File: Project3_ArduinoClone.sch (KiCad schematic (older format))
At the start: 13 parts, among them U1 24LC1025, U2 24LC1025, U3 DS1337_v1, U4 ATMEGA328P-AU, Y1 Crystal, Y2 Crystal

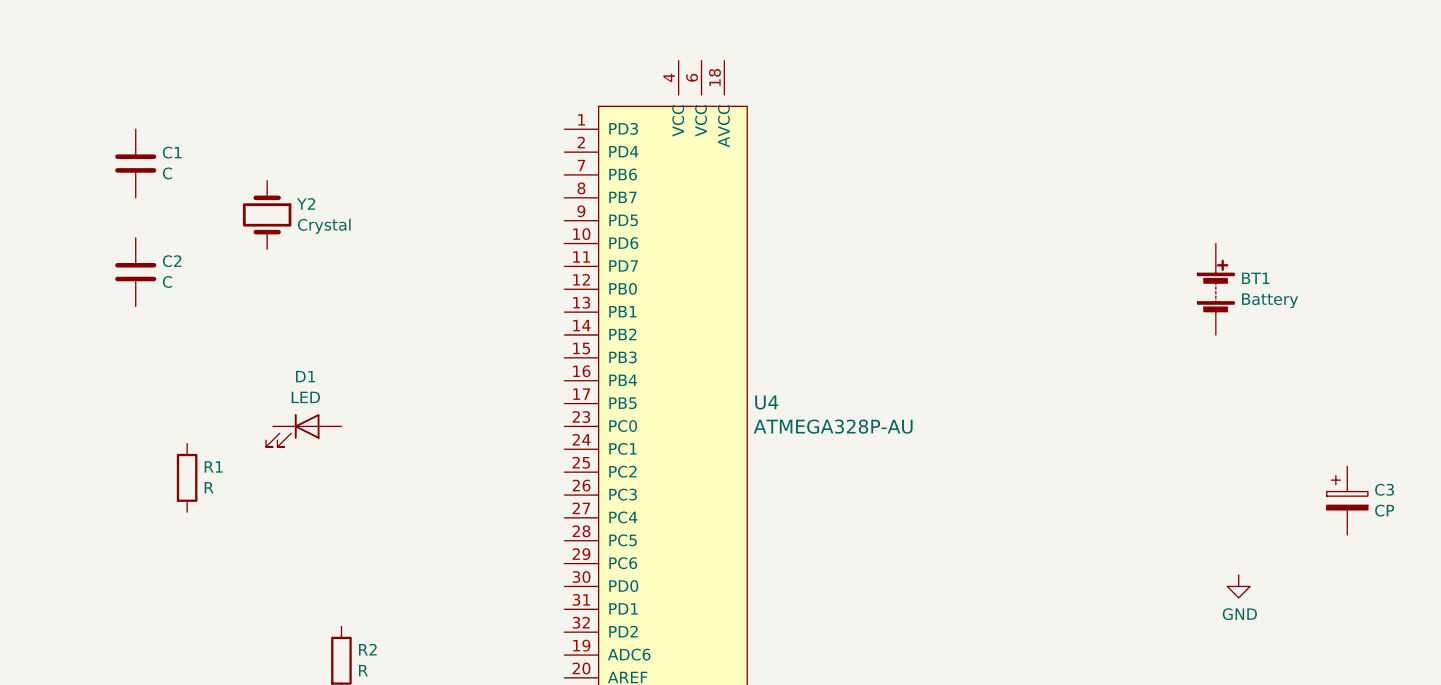
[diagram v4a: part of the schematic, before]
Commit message: Footprints assigned.
Review with real footprints that I'm going to use.
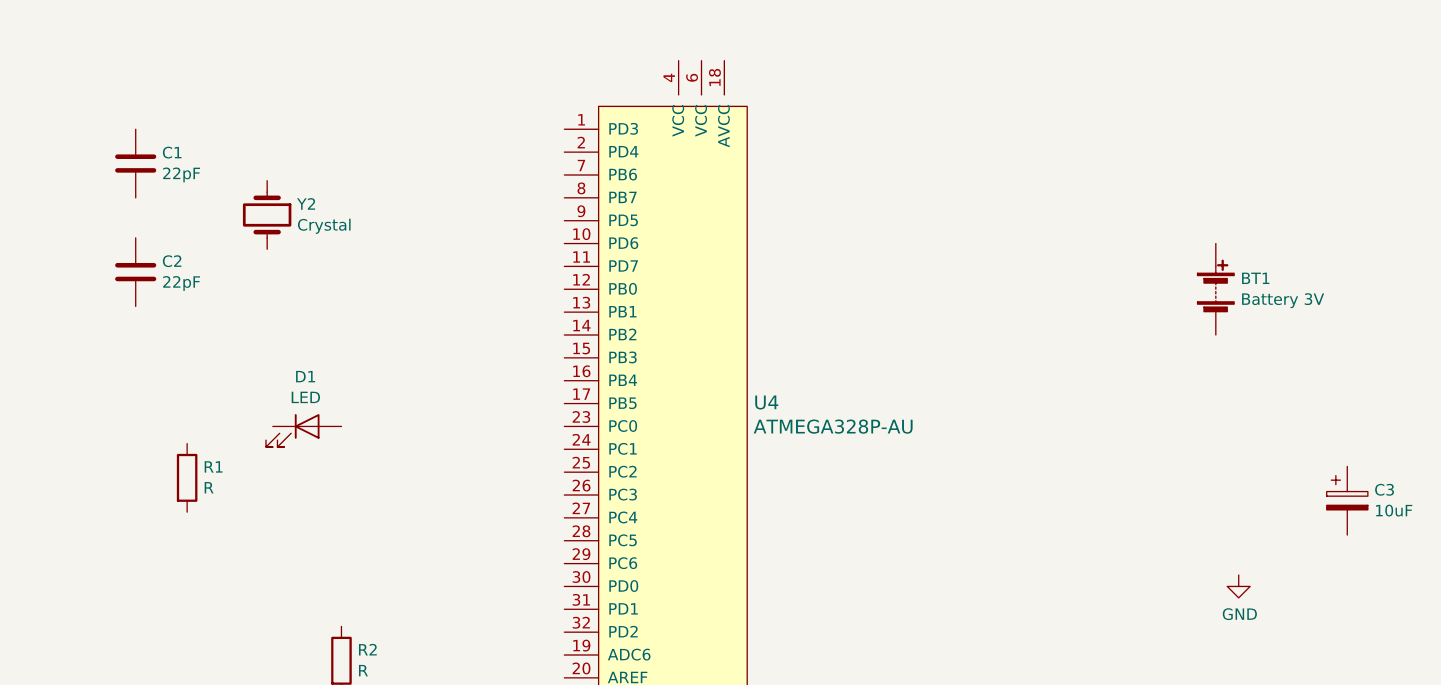
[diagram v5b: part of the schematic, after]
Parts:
- BT1: value Battery -> Battery 3V; footprint (none) -> Connector_PinHeader_2.54mm:PinHeader_1x02_P2.54mm_Vertical
- C1, C2: value C -> 22pF; footprint (none) -> Capacitor_SMD:C_0805_2012Metric_Pad1.15x1.40mm_HandSolder
- C3: value CP -> 10uF; footprint (none) -> Capacitor_SMD:C_0805_2012Metric_Pad1.15x1.40mm_HandSolder
- D1: footprint (none) -> LED_SMD:LED_0805_2012Metric_Pad1.15x1.40mm_HandSolder
- R1, R2: footprint (none) -> Resistor_SMD:R_0805_2012Metric_Pad1.15x1.40mm_HandSolder
- U1, U2: footprint (none) -> Package_SO:SOIJ-8_5.3x5.3mm_P1.27mm
- U3: footprint (none) -> Package_SO:SO-8_5.3x6.2mm_P1.27mm
- Y1: footprint (none) -> Crystal:Crystal_SMD_MicroCrystal_CC7V-T1A-2Pin_3.2x1.5mm_HandSoldering
- Y2: footprint (none) -> Crystal:Crystal_SMD_5032-2Pin_5.0x3.2mm_HandSoldering
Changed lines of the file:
@@
 P 9450 2975
 F 0 "BT1" H 9558 3021 50  0000 L CNN
-F 1 "Battery" H 9558 2930 50  0000 L CNN
-F 2 "" V 9450 3035 50  0001 C CNN
+F 1 "Battery 3V" H 9558 2930 50  0000 L CNN
+F 2 "Connector_PinHeader_2.54mm:PinHeader_1x02_P2.54mm_Vertical" V 9450 3035 50  0001 C CNN
 F 3 "~" V 9450 3035 50  0001 C CNN
 	1    9450 2975
@@
 P 4725 2425
 F 0 "C1" H 4840 2471 50  0000 L CNN
-F 1 "C" H 4840 2380 50  0000 L CNN
-F 2 "" H 4763 2275 50  0001 C CNN
+F 1 "22pF" H 4840 2380 50  0000 L CNN
+F 2 "Capacitor_SMD:C_0805_2012Metric_Pad1.15x1.40mm_HandSolder" H 4763 2275 50  0001 C CNN
 F 3 "~" H 4725 2425 50  0001 C CNN
 	1    4725 2425
@@
 P 4725 2900
 F 0 "C2" H 4840 2946 50  0000 L CNN
-F 1 "C" H 4840 2855 50  0000 L CNN
-F 2 "" H 4763 2750 50  0001 C CNN
+F 1 "22pF" H 4840 2855 50  0000 L CNN
+F 2 "Capacitor_SMD:C_0805_2012Metric_Pad1.15x1.40mm_HandSolder" H 4763 2750 50  0001 C CNN
 F 3 "~" H 4725 2900 50  0001 C CNN
 	1    4725 2900
@@
 P 10025 3900
 F 0 "C3" H 10143 3946 50  0000 L CNN
-F 1 "CP" H 10143 3855 50  0000 L CNN
-F 2 "" H 10063 3750 50  0001 C CNN
+F 1 "10uF" H 10143 3855 50  0000 L CNN
+F 2 "Capacitor_SMD:C_0805_2012Metric_Pad1.15x1.40mm_HandSolder" H 10063 3750 50  0001 C CNN
 F 3 "~" H 10025 3900 50  0001 C CNN
 	1    10025 3900
@@
 F 0 "D1" H 5468 3791 50  0000 C CNN
 F 1 "LED" H 5468 3700 50  0000 C CNN
-F 2 "" H 5475 3575 50  0001 C CNN
+F 2 "LED_SMD:LED_0805_2012Metric_Pad1.15x1.40mm_HandSolder" H 5475 3575 50  0001 C CNN
 F 3 "~" H 5475 3575 50  0001 C CNN
 	1    5475 3575
@@
 F 0 "R1" H 5020 3846 50  0000 L CNN
 F 1 "R" H 5020 3755 50  0000 L CNN
-F 2 "" V 4880 3800 50  0001 C CNN
+F 2 "Resistor_SMD:R_0805_2012Metric_Pad1.15x1.40mm_HandSolder" V 4880 3800 50  0001 C CNN
 F 3 "~" H 4950 3800 50  0001 C CNN
 	1    4950 3800
@@
 F 0 "R2" H 5695 4646 50  0000 L CNN
 F 1 "R" H 5695 4555 50  0000 L CNN
-F 2 "" V 5555 4600 50  0001 C CNN
+F 2 "Resistor_SMD:R_0805_2012Metric_Pad1.15x1.40mm_HandSolder" V 5555 4600 50  0001 C CNN
 F 3 "~" H 5625 4600 50  0001 C CNN
 	1    5625 4600
@@
 F 0 "U1" H 1825 4931 50  0000 C CNN
 F 1 "24LC1025" H 1825 4840 50  0000 C CNN
-F 2 "" H 1825 4450 50  0001 C CNN
+F 2 "Package_SO:SOIJ-8_5.3x5.3mm_P1.27mm" H 1825 4450 50  0001 C CNN
 F 3 "http://ww1.microchip.com/downloads/en/DeviceDoc/21941B.pdf" H 1825 4450 50  0001 C CNN
 	1    1825 4450
@@
 F 0 "U3" H 2625 2481 50  0000 C CNN
 F 1 "DS1337_v1" H 2625 2390 50  0000 C CNN
-F 2 "" H 2625 1850 50  0001 C CNN
+F 2 "Package_SO:SO-8_5.3x6.2mm_P1.27mm" H 2625 1850 50  0001 C CNN
 F 3 "https://datasheets.maximintegrated.com/en/ds/DS1337-DS1337C.pdf" H 2625 1850 50  0001 C CNN
 	1    2625 1850
@@
 F 0 "Y1" V 1554 1881 50  0000 L CNN
 F 1 "Crystal" V 1645 1881 50  0000 L CNN
-F 2 "" H 1600 1750 50  0001 C CNN
+F 2 "Crystal:Crystal_SMD_MicroCrystal_CC7V-T1A-2Pin_3.2x1.5mm_HandSoldering" H 1600 1750 50  0001 C CNN
 F 3 "~" H 1600 1750 50  0001 C CNN
 	1    1600 1750
@@
 F 0 "Y2" V 5254 2781 50  0000 L CNN
 F 1 "Crystal" V 5345 2781 50  0000 L CNN
-F 2 "" H 5300 2650 50  0001 C CNN
+F 2 "Crystal:Crystal_SMD_5032-2Pin_5.0x3.2mm_HandSoldering" H 5300 2650 50  0001 C CNN
 F 3 "~" H 5300 2650 50  0001 C CNN
 	1    5300 2650
@@
 F 0 "U2" H 1825 5806 50  0000 C CNN
 F 1 "24LC1025" H 1825 5715 50  0000 C CNN
-F 2 "" H 1825 5325 50  0001 C CNN
+F 2 "Package_SO:SOIJ-8_5.3x5.3mm_P1.27mm" H 1825 5325 50  0001 C CNN
 F 3 "http://ww1.microchip.com/downloads/en/DeviceDoc/21941B.pdf" H 1825 5325 50  0001 C CNN
 	1    1825 5325

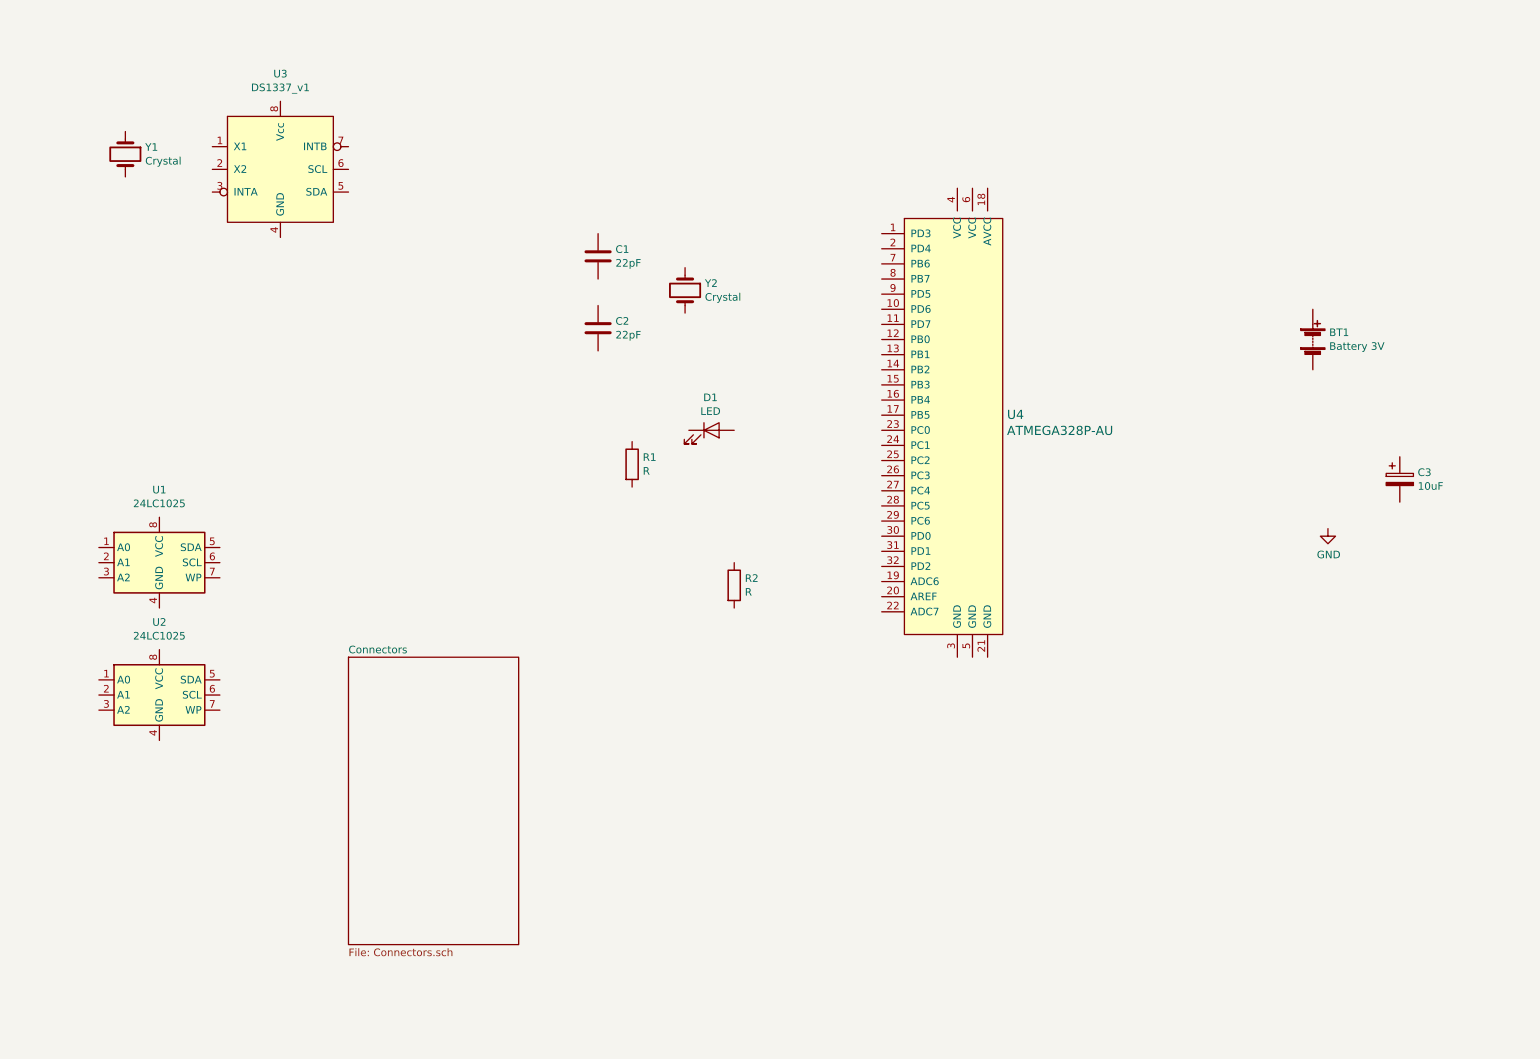
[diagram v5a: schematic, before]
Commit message: Place labels on connectors sheet & wire
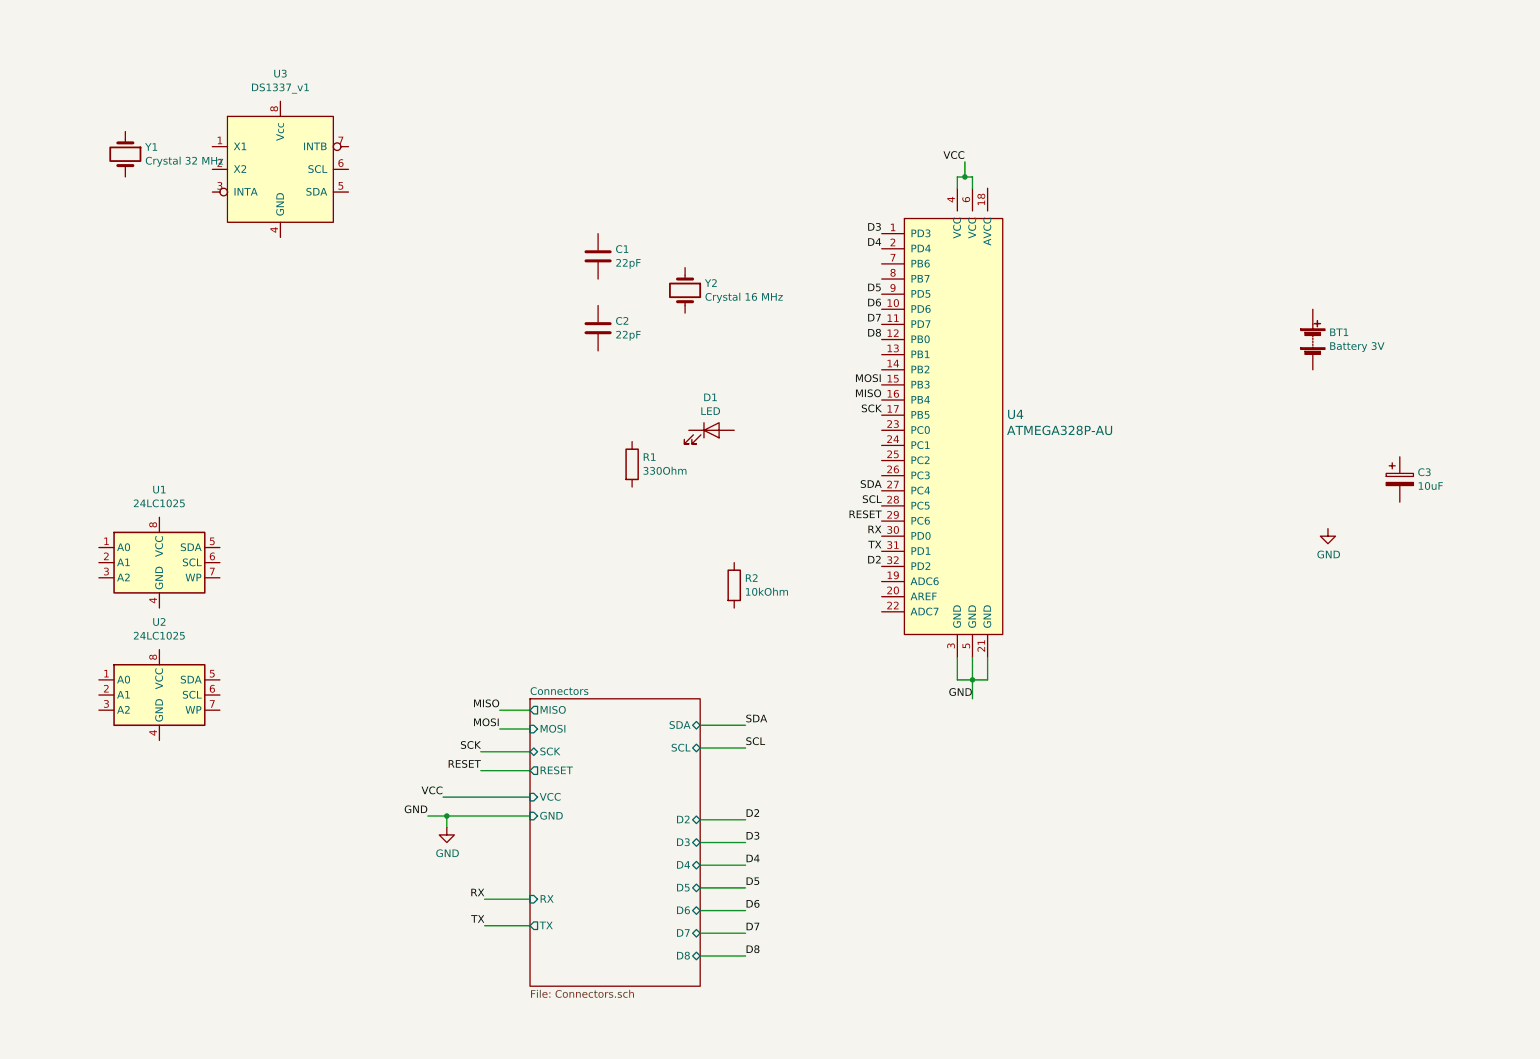
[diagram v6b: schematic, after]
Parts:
- R1: value R -> 330Ohm
- R2: value R -> 10kOhm
- Y1: value Crystal -> Crystal 32 MHz
- Y2: value Crystal -> Crystal 16 MHz
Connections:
- net GND: now also U4.21 (GND), U4.3 (GND), U4.5 (GND)
- net D3: now reaches U4.1 (PD3)
- net D6: now reaches U4.10 (PD6)
- net D7: now reaches U4.11 (PD7)
- net D8: now reaches U4.12 (PB0)
- net MOSI: now reaches U4.15 (PB3)
- net MISO: now reaches U4.16 (PB4)
- net SCK: now reaches U4.17 (PB5)
- net D4: now reaches U4.2 (PD4)
- net SDA: now reaches U4.27 (PC4)
- net SCL: now reaches U4.28 (PC5)
- net RESET: now reaches U4.29 (PC6)
- net RX: now reaches U4.30 (PD0)
- net TX: now reaches U4.31 (PD1)
- net D2: now reaches U4.32 (PD2)
- net VCC: now reaches U4.4 (VCC)
- net VCC: now also U4.6 (VCC)
- net D5: now reaches U4.9 (PD5)
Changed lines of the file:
@@
 P 4950 3800
 F 0 "R1" H 5020 3846 50  0000 L CNN
-F 1 "R" H 5020 3755 50  0000 L CNN
+F 1 "330Ohm" H 5020 3755 50  0000 L CNN
 F 2 "Resistor_SMD:R_0805_2012Metric_Pad1.15x1.40mm_HandSolder" V 4880 3800 50  0001 C CNN
 F 3 "~" H 4950 3800 50  0001 C CNN
@@
 P 5625 4600
 F 0 "R2" H 5695 4646 50  0000 L CNN
-F 1 "R" H 5695 4555 50  0000 L CNN
+F 1 "10kOhm" H 5695 4555 50  0000 L CNN
 F 2 "Resistor_SMD:R_0805_2012Metric_Pad1.15x1.40mm_HandSolder" V 5555 4600 50  0001 C CNN
 F 3 "~" H 5625 4600 50  0001 C CNN
@@
 	1    0    0    -1
 $EndComp
-$Sheet
-S 3075 5075 1125 1900
-U 5DA33D85
-F0 "Connectors" 50
-F1 "Connectors.sch" 50
-$EndSheet
 $Comp
 L dk_Embedded-Microcontrollers:ATMEGA328P-AU U4
@@
 P 1600 1750
 F 0 "Y1" V 1554 1881 50  0000 L CNN
-F 1 "Crystal" V 1645 1881 50  0000 L CNN
+F 1 "Crystal 32 MHz" V 1645 1881 50  0000 L CNN
 F 2 "Crystal:Crystal_SMD_MicroCrystal_CC7V-T1A-2Pin_3.2x1.5mm_HandSoldering" H 1600 1750 50  0001 C CNN
 F 3 "~" H 1600 1750 50  0001 C CNN
@@
 P 5300 2650
 F 0 "Y2" V 5254 2781 50  0000 L CNN
-F 1 "Crystal" V 5345 2781 50  0000 L CNN
+F 1 "Crystal 16 MHz" V 5345 2781 50  0000 L CNN
 F 2 "Crystal:Crystal_SMD_5032-2Pin_5.0x3.2mm_HandSoldering" H 5300 2650 50  0001 C CNN
 F 3 "~" H 5300 2650 50  0001 C CNN
@@
 	1    0    0    -1
 $EndComp
+Text Label 4075 5425 2    50   ~ 0
+MISO
+Wire Wire Line
+	4075 5550 4275 5550
+Text Label 6600 3375 2    50   ~ 0
+MISO
+Text Label 3950 5700 2    50   ~ 0
+SCK
+Text Label 3700 6000 2    50   ~ 0
+VCC
+Text Label 3950 5825 2    50   ~ 0
+RESET
+Text Label 4075 5550 2    50   ~ 0
+MOSI
+Text Label 3600 6125 2    50   ~ 0
+GND
+Wire Wire Line
+	3950 5700 4275 5700
+Wire Wire Line
+	4075 5425 4275 5425
+Wire Wire Line
+	4275 5825 3950 5825
+Wire Wire Line
+	3700 6000 4275 6000
+Wire Wire Line
+	3600 6125 3725 6125
+Text Label 7200 5350 2    50   ~ 0
+GND
+Wire Wire Line
+	7100 5225 7100 5075
+Wire Wire Line
+	7100 5225 7200 5225
+Wire Wire Line
+	7300 5225 7300 5075
+Wire Wire Line
+	7200 5075 7200 5225
+Connection ~ 7200 5225
+Wire Wire Line
+	7200 5225 7300 5225
+Wire Wire Line
+	7200 5350 7200 5225
+Text Label 7150 1800 2    50   ~ 0
+VCC
+Wire Wire Line
+	7100 1975 7100 1900
+Wire Wire Line
+	7100 1900 7150 1900
+Wire Wire Line
+	7200 1900 7200 1975
+Connection ~ 7150 1900
+Wire Wire Line
+	7150 1900 7200 1900
+Wire Wire Line
+	7150 1800 7150 1900
+Text Label 6600 3275 2    50   ~ 0
+MOSI
+Text Label 6600 3475 2    50   ~ 0
+SCK
+Text Label 6600 4175 2    50   ~ 0
+RESET
+$Comp
+L power:GND #PWR?
+U 1 1 5DA57C48
+P 3725 6200
+F 0 "#PWR?" H 3725 5950 50  0001 C CNN
+F 1 "GND" H 3730 6027 50  0000 C CNN
+F 2 "" H 3725 6200 50  0001 C CNN
+F 3 "" H 3725 6200 50  0001 C CNN
+	1    3725 6200
+	1    0    0    -1
+$EndComp
+Wire Wire Line
+	3725 6200 3725 6125
+Connection ~ 3725 6125
+Wire Wire Line
+	3725 6125 4275 6125
+$Sheet
+S 4275 5350 1125 1900
+U 5DA33D85
+F0 "Connectors" 50
+F1 "Connectors.sch" 50
+F2 "MISO" O L 4275 5425 50
+F3 "SCK" B L 4275 5700 50
+F4 "VCC" I L 4275 6000 50
+F5 "RESET" O L 4275 5825 50
+F6 "MOSI" I L 4275 5550 50
+F7 "GND" I L 4275 6125 50
+F8 "RX" I L 4275 6675 50
+F9 "TX" O L 4275 6850 50
+F10 "SDA" B R 5400 5525 50
+F11 "SCL" B R 5400 5675 50
+F12 "D2" B R 5400 6150 50
+F13 "D3" B R 5400 6300 50
+F14 "D4" B R 5400 6450 50
+F15 "D5" B R 5400 6600 50
+F16 "D6" B R 5400 6750 50
+F17 "D7" B R 5400 6900 50
+F18 "D8" B R 5400 7050 50
+$EndSheet
+Text Label 5700 5525 0    50   ~ 0
+SDA
+Text Label 5700 5675 0    50   ~ 0
+SCL
+Text Label 5700 6150 0    50   ~ 0
+D2
+Text Label 5700 6300 0    50   ~ 0
+D3
+Text Label 5700 6450 0    50   ~ 0
+D4
+Text Label 5700 6600 0    50   ~ 0
+D5
+Text Label 5700 6750 0    50   ~ 0
+D6
+Text Label 5700 6900 0    50   ~ 0
+D7
+Text Label 5700 7050 0    50   ~ 0
+D8
+Wire Wire Line
+	5400 5525 5700 5525
+Wire Wire Line
+	5700 5675 5400 5675
+Wire Wire Line
+	5400 6150 5700 6150
+Wire Wire Line
+	5400 6300 5700 6300
+Wire Wire Line
+	5700 6450 5400 6450
+Wire Wire Line
+	5400 6600 5700 6600
+Wire Wire Line
+	5700 6750 5400 6750
+Wire Wire Line
+	5400 6900 5700 6900
+Wire Wire Line
+	5700 7050 5400 7050
+Text Label 3975 6675 2    50   ~ 0
+RX
+Text Label 3975 6850 2    50   ~ 0
+TX
+Wire Wire Line
+	3975 6675 4275 6675
+Wire Wire Line
+	3975 6850 4275 6850
+Text Label 6600 2275 2    50   ~ 0
+D3
+Text Label 6600 2375 2    50   ~ 0
+D4
+Text Label 6600 2675 2    50   ~ 0
+D5
+Text Label 6600 2775 2    50   ~ 0
+D6
+Text Label 6600 2875 2    50   ~ 0
+D7
+Text Label 6600 2975 2    50   ~ 0
+D8
+Text Label 6600 3975 2    50   ~ 0
+SDA
+Text Label 6600 4075 2    50   ~ 0
+SCL
+Text Label 6600 4275 2    50   ~ 0
+RX
+Text Label 6600 4375 2    50   ~ 0
+TX
+Text Label 6600 4475 2    50   ~ 0
+D2
 $EndSCHEMATC
